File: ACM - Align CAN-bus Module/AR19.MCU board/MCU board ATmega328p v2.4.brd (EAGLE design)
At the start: 160 x 100 mm, 37 parts, among them IC1 ATMEGA328P-MMH, IC2 MIC5239-5.0YS_TR, IC3 MCP25625-E_ML, J1 AVR_SPI_PROG_3X2NS

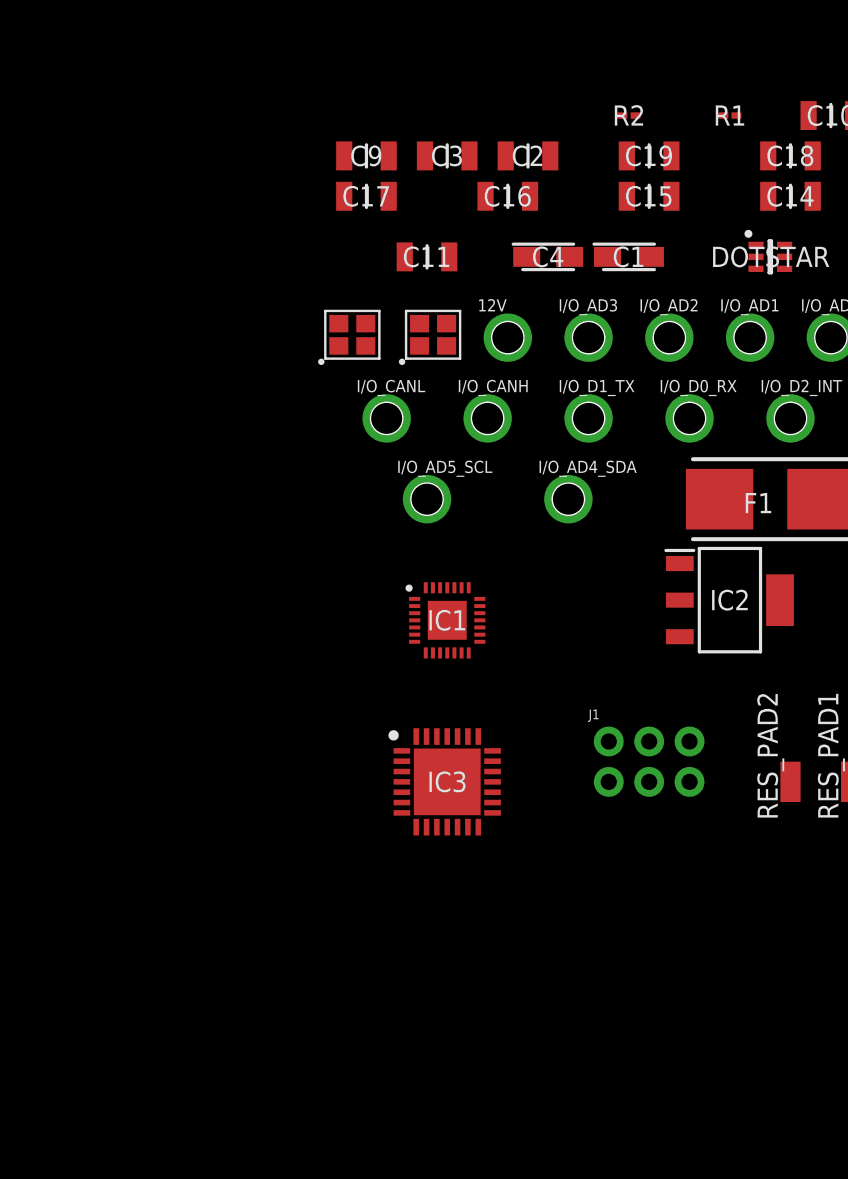
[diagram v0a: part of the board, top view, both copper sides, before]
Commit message: + SPI Priority | / 10K and 500Ohm to larger package | Smallest part 1206
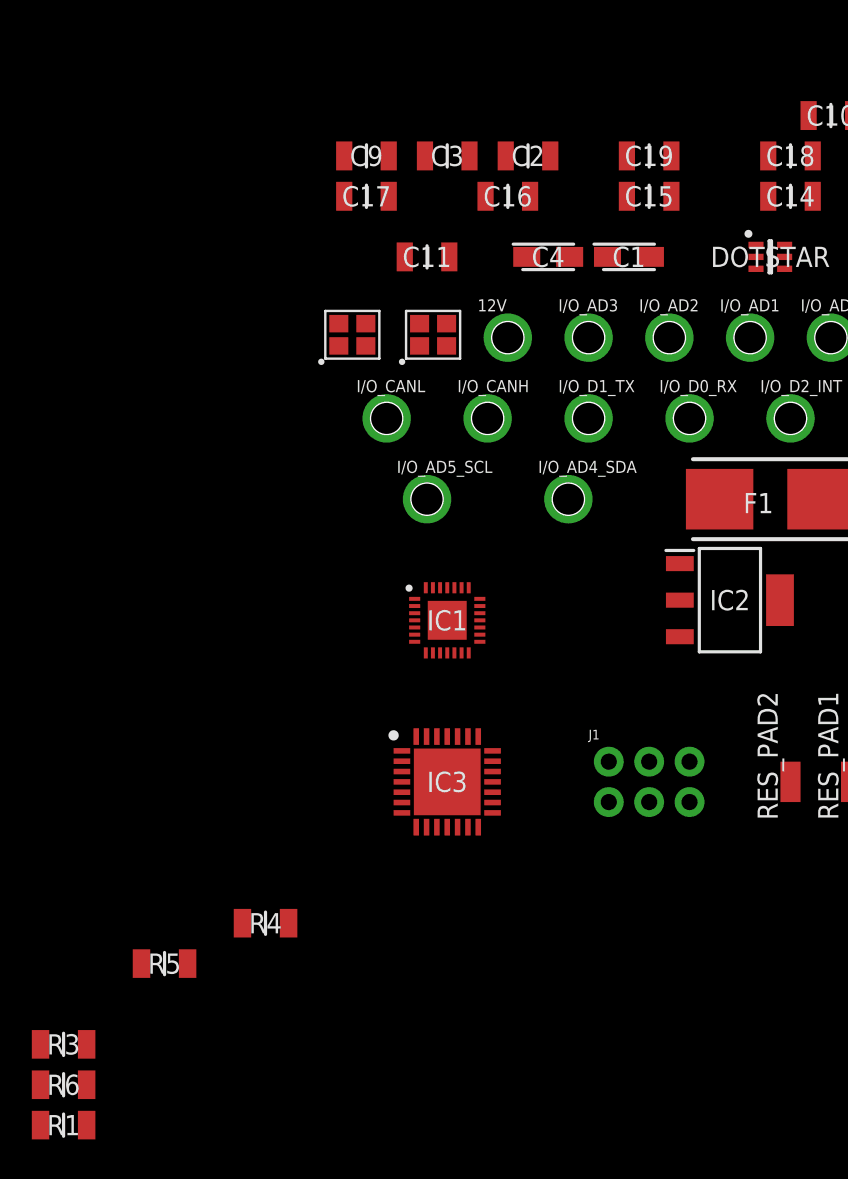
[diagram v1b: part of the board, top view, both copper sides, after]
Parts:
- removed R2: 10KΩ, CPF0201D10KC1:RESC0603X28N
- added R3, R4, R5: 500Ohm, CRCW1206499RFKEAHP(499ohm resistor):RESC3116X65N
- added R6: 10K Ohm, CRCW120610K0FKEAHP(10K Ohm):RESC3116X65N
- R1: value 10KΩ -> 10K Ohm; device CPF0201D10KC1:RESC0603X28N -> CRCW120610K0FKEAHP(10K Ohm):RESC3116X65N
- moved R1 76.1 mm to (-63.5, -17.8)
- moved J1 1.27 mm to (-26.7, 3.81)
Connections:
- removed net MISO: J1.1
- removed net MOSI: J1.4
- new net PROG_MISO: J1.1, R4.1
- new net PROG_MOSI: J1.4, R5.1
- new net PROG_SCK: J1.3, R3.1
- net 5V: now also R6.2; no longer R2.2
- net CAN_MISO: now also R4.2
- net CAN_MOSI: now also R5.2
- net MCP_RESET: now also R1.1; no longer R2.1
- net RESET_MCU: now also R6.1; no longer R1.1
- net SCK: now also R3.2; no longer J1.3

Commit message: Updated BOM and SPI Priority
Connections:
- net CAN_MISO: now also R4.1; no longer IC1.14, R4.2
- net CAN_MOSI: now also R5.1; no longer IC1.13, R5.2
- net PROG_MISO: now also IC1.14, R4.2; no longer R4.1
- net PROG_MOSI: now also IC1.13, R5.2; no longer R5.1
- net PROG_SCK: now also IC1.15, R3.2; no longer R3.1
- net SCK: now also R3.1; no longer IC1.15, R3.2
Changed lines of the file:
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@@
 </signal>
 <signal name="SCK">
-<contactref element="IC1" pad="15"/>
 <contactref element="DOTSTAR" pad="2"/>
 <contactref element="IC3" pad="26"/>
-<contactref element="R3" pad="2"/>
-<wire x1="-40.02" y1="6.66" x2="-62.05" y2="-12.7" width="0" layer="19" extent="1-1"/>
-<wire x1="-37.32" y1="12.62" x2="-40.02" y2="6.66" width="0" layer="19" extent="1-1"/>
-<wire x1="-19.95" y1="36.83" x2="-37.32" y2="12.62" width="0" layer="19" extent="1-1"/>
+<contactref element="R3" pad="1"/>
+<wire x1="-40.02" y1="6.66" x2="-64.95" y2="-12.7" width="0" layer="19" extent="1-1"/>
+<wire x1="-19.95" y1="36.83" x2="-40.02" y2="6.66" width="0" layer="19" extent="1-1"/>
 </signal>
 <signal name="CANL">
@@
 <signal name="CAN_MISO">
 <contactref element="IC3" pad="28"/>
-<contactref element="IC1" pad="14"/>
-<contactref element="R4" pad="2"/>
-<wire x1="-41.32" y1="6.66" x2="-49.35" y2="-5.08" width="0" layer="19" extent="1-1"/>
-<wire x1="-38.02" y1="11.92" x2="-41.32" y2="6.66" width="0" layer="19" extent="1-1"/>
+<contactref element="R4" pad="1"/>
+<wire x1="-41.32" y1="6.66" x2="-52.25" y2="-5.08" width="0" layer="19" extent="1-1"/>
 </signal>
 <signal name="CAN_MOSI">
 <contactref element="IC3" pad="27"/>
-<contactref element="IC1" pad="13"/>
-<contactref element="R5" pad="2"/>
-<wire x1="-40.67" y1="6.66" x2="-55.7" y2="-7.62" width="0" layer="19" extent="1-1"/>
-<wire x1="-38.47" y1="11.92" x2="-40.67" y2="6.66" width="0" layer="19" extent="1-1"/>
+<contactref element="R5" pad="1"/>
+<wire x1="-40.67" y1="6.66" x2="-58.6" y2="-7.62" width="0" layer="19" extent="1-1"/>
 </signal>
 <signal name="TXCAN">
@@
 </signal>
 <signal name="PROG_MISO">
-<contactref element="R4" pad="1"/>
 <contactref element="J1" pad="1"/>
-<wire x1="-29.21" y1="2.54" x2="-52.25" y2="-5.08" width="0" layer="19" extent="1-1"/>
+<contactref element="IC1" pad="14"/>
+<contactref element="R4" pad="2"/>
+<wire x1="-38.02" y1="11.92" x2="-49.35" y2="-5.08" width="0" layer="19" extent="1-1"/>
+<wire x1="-29.21" y1="2.54" x2="-38.02" y2="11.92" width="0" layer="19" extent="1-1"/>
 </signal>
 <signal name="PROG_MOSI">
-<contactref element="R5" pad="1"/>
 <contactref element="J1" pad="4"/>
-<wire x1="-26.67" y1="5.08" x2="-58.6" y2="-7.62" width="0" layer="19" extent="1-1"/>
+<contactref element="IC1" pad="13"/>
+<contactref element="R5" pad="2"/>
+<wire x1="-38.47" y1="11.92" x2="-55.7" y2="-7.62" width="0" layer="19" extent="1-1"/>
+<wire x1="-26.67" y1="5.08" x2="-38.47" y2="11.92" width="0" layer="19" extent="1-1"/>
 </signal>
 <signal name="PROG_SCK">
-<contactref element="R3" pad="1"/>
 <contactref element="J1" pad="3"/>
-<wire x1="-26.67" y1="2.54" x2="-64.95" y2="-12.7" width="0" layer="19" extent="1-1"/>
+<contactref element="IC1" pad="15"/>
+<contactref element="R3" pad="2"/>
+<wire x1="-37.32" y1="12.62" x2="-62.05" y2="-12.7" width="0" layer="19" extent="1-1"/>
+<wire x1="-26.67" y1="2.54" x2="-37.32" y2="12.62" width="0" layer="19" extent="1-1"/>
 </signal>
 </signals>

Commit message: New board
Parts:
- moved IC2 66.5 mm to (39.4, 41.9)
- moved C4 57.2 mm to (24.1, 39.4), turned to 90 degrees
- moved IC3 55.8 mm to (14.0, 20.3)
- moved IC1 54.6 mm to (12.7, 30.5)
- moved DOTSTAR 50.8 mm to (21.6, 6.35)
- moved F1 41.7 mm to (14.0, 47.0)
- moved J1 39.5 mm to (12.7, 6.35)
- moved 12V 31.9 mm to (-6.35, 44.5)
- moved R4 15.7 mm to (-35.6, -8.89)
- moved C1 9.67 mm to (-19.1, 33.0)
- moved C16 1.80 mm to (-34.3, 39.4)

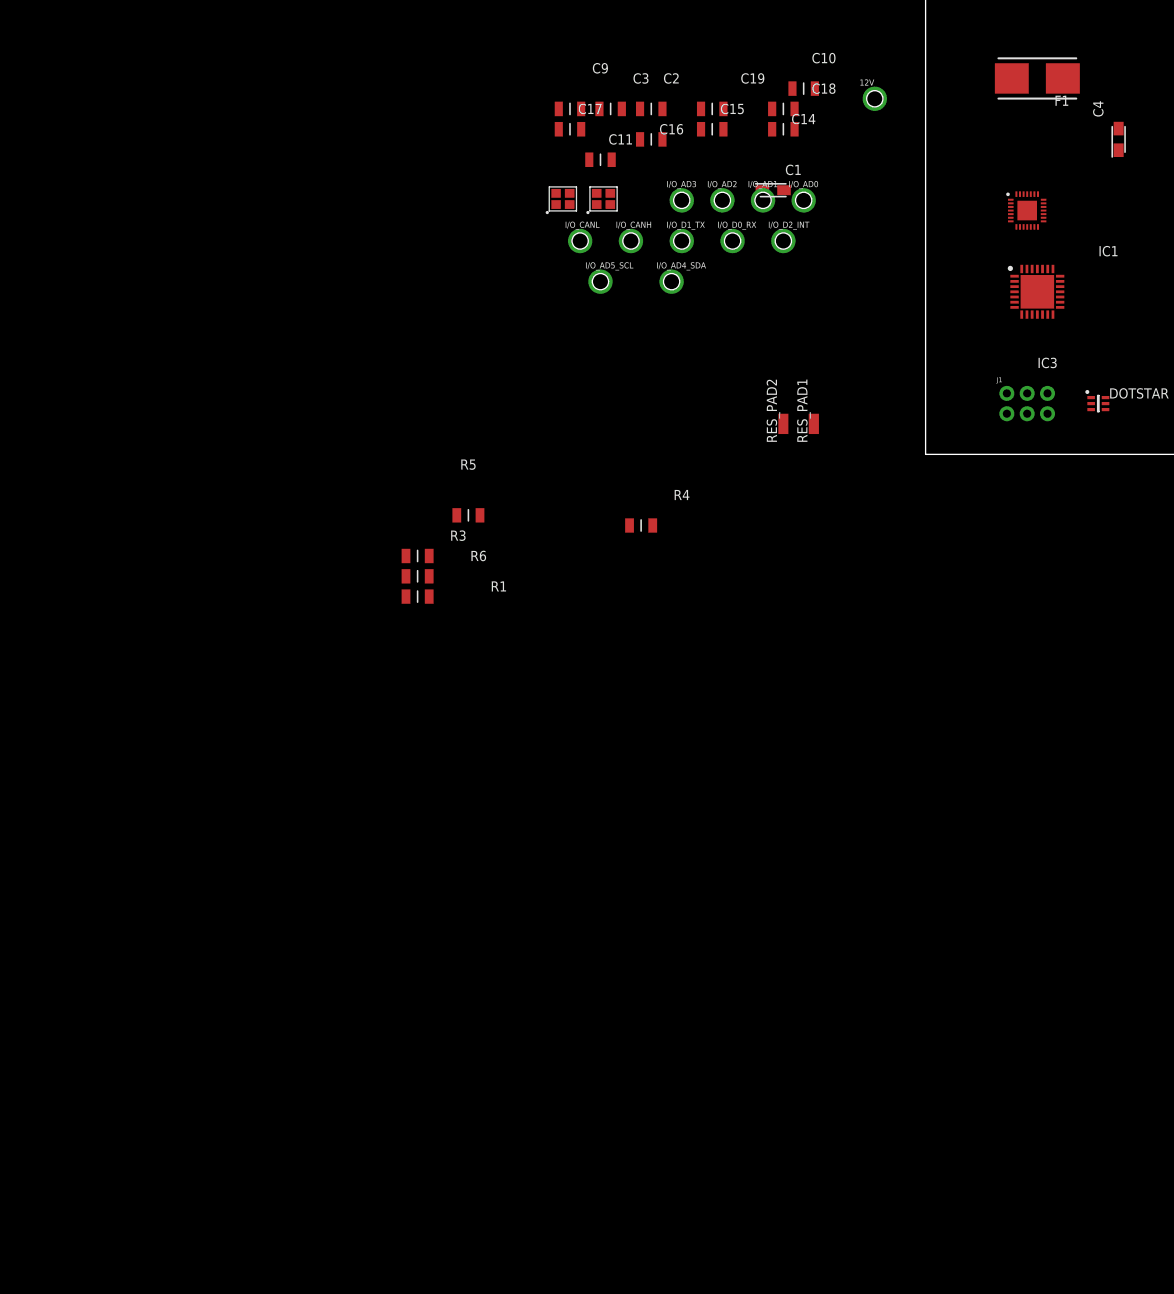
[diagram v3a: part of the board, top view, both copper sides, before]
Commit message: Byttet I/O pins, 0603 imp smd størrelse. Mangler dotstar support
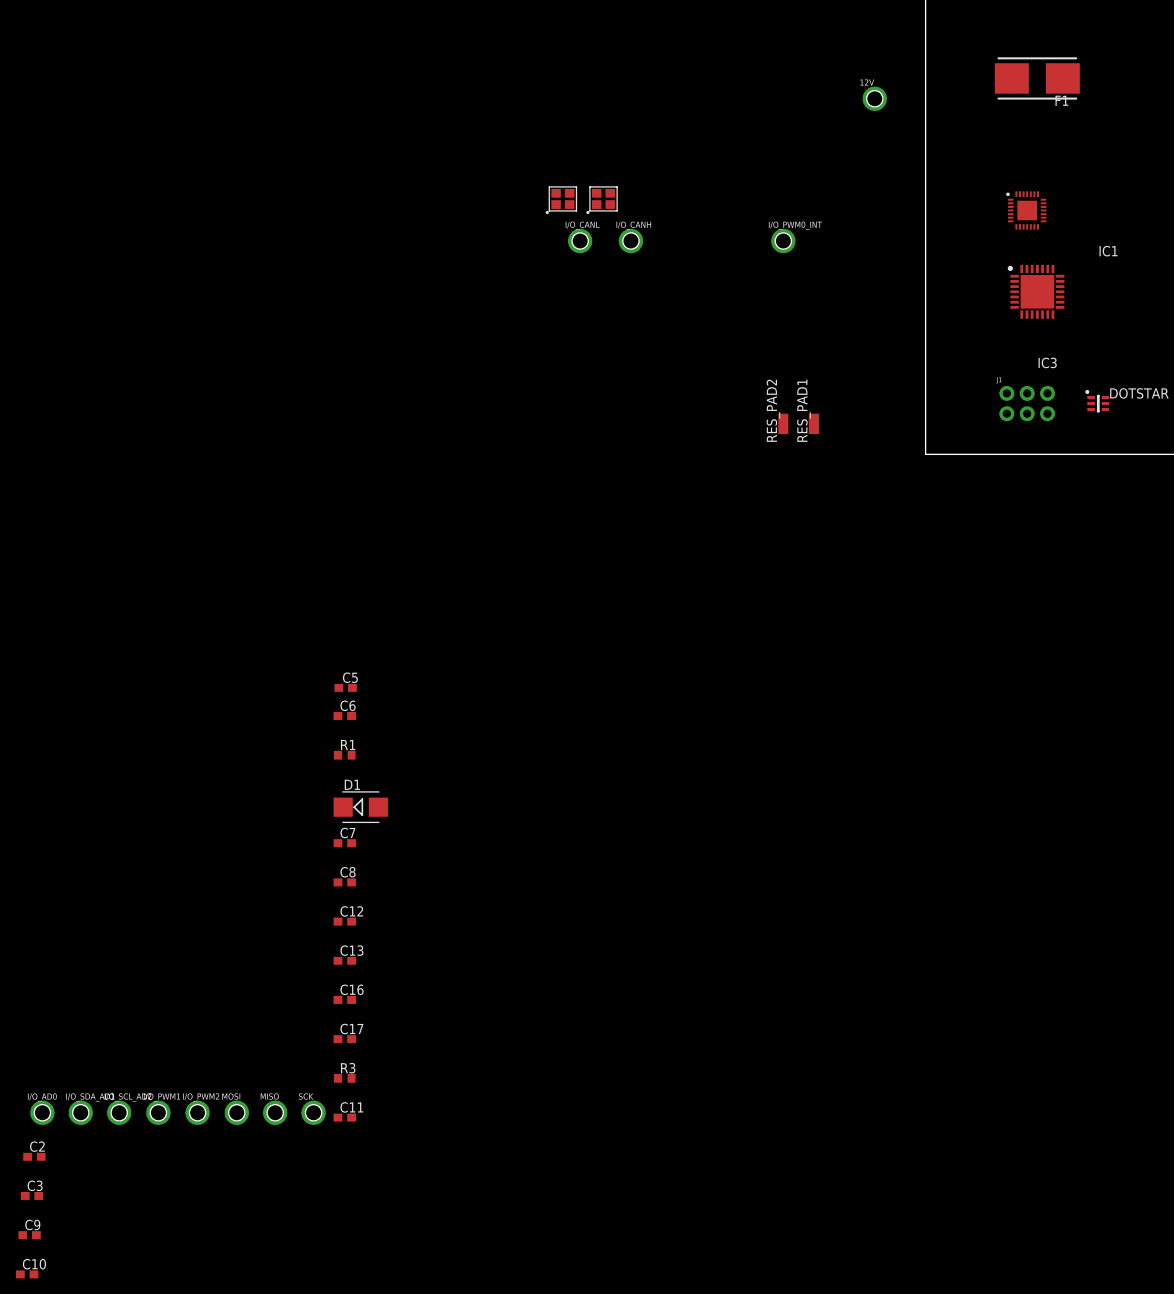
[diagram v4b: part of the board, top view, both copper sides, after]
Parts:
- removed C1, C4: 10uF, T491A106K016AT:CAPPM3216X180N
- removed C14, C15, C18, C19: 0.1uF_12, 12066D106KAT2A:CAPC3216X229N
- removed I/O_AD1, I/O_AD2, I/O_AD3, I/O_AD4_SDA, I/O_AD5_SCL, I/O_D0_RX, I/O_D1_TX: (no value), wirepad_edit:2,54/2,0(HALFHOLE)H+V
- removed R4, R5: 500Ohm, CRCW1206499RFKEAHP(499ohm resistor):RESC3116X65N
- removed R6: 10K Ohm, CRCW120610K0FKEAHP(10K Ohm):RESC3116X65N
- added C12, C13, C6, C7, C8: 0.1uF, eagle-ltspice:C0603
- added C5: 22pF, eagle-ltspice:C0603
- added D1: (no value), eagle-ltspice:DIODE_SMB
- added I/O_PWM1: I/O_PWM1, wirepad_edit:2,54/2,0(HALFHOLE)H+V
- added I/O_PWM2: I/O_PWM2, wirepad_edit:2,54/2,0(HALFHOLE)H+V
- added I/O_SCL_AD2: I/O_SCL_AD2, wirepad_edit:2,54/2,0(HALFHOLE)H+V
- added I/O_SDA_AD1: I/O_SDA_AD1, wirepad_edit:2,54/2,0(HALFHOLE)H+V
- added MISO: MISO, wirepad_edit:2,54/2,0(HALFHOLE)H+V
- added MOSI: MOSI, wirepad_edit:2,54/2,0(HALFHOLE)H+V
- added SCK: SCK, wirepad_edit:2,54/2,0(HALFHOLE)H+V
- 12V: value (none) -> 12V
- C10: value 22pF -> 10uF; device 12066D106KAT2A:CAPC3216X229N -> eagle-ltspice:C0603
- C11: value 0.1uF_12 -> 10uF; device 12066D106KAT2A:CAPC3216X229N -> eagle-ltspice:C0603
- C16, C17: value 0.1uF_12 -> 0.1uF; device 12066D106KAT2A:CAPC3216X229N -> eagle-ltspice:C0603
- C2, C3, C9: device 12066D106KAT2A:CAPC3216X229N -> eagle-ltspice:C0603
- I/O_AD0: value (none) -> I/O_AD0
- I/O_CANH, I/O_CANL: value (none) -> I/O_CANH
- I/O_PWM0_INT: value (none) -> I/O_PWM0_INT
- R1: value 10K Ohm -> 10kOhm; device CRCW120610K0FKEAHP(10K Ohm):RESC3116X65N -> eagle-ltspice:R0603
- R3: value 500Ohm -> 10kOhm; device CRCW1206499RFKEAHP(499ohm resistor):RESC3116X65N -> eagle-ltspice:R0603
- RES_PAD1: value (none) -> RES_PAD
- RES_PAD2: value (none) -> RES_PAD2
- moved C10 177.2 mm to (-112.3, -102.5)
- moved C9 156.1 mm to (-112.0, -97.6)
- moved C3 153.9 mm to (-111.7, -92.7)
- moved C2 152.0 mm to (-111.4, -87.8)
- moved I/O_AD0 148.5 mm to (-110.4, -82.3)
- moved C11 123.9 mm to (-72.6, -82.9)
- moved C17 117.2 mm to (-72.6, -73.1)
- moved C16 114.2 mm to (-72.6, -68.2)
- moved R3 65.9 mm to (-72.6, -78.0)
- moved R1 21.8 mm to (-72.6, -37.6)
- renumbered I/O_D2_INT to I/O_PWM0_INT
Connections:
- net CAN_INIT renamed CAN_INT
- removed net CAN_MISO: IC3.28, R4.1
- removed net CAN_MOSI: IC3.27, R5.1
- removed net I/O_AD0: I/O_AD0.P$1, IC1.19
- removed net I/O_AD1: I/O_AD1.P$1, IC1.20
- removed net I/O_AD2: I/O_AD2.P$1, IC1.21
- removed net I/O_AD3: I/O_AD3.P$1, IC1.22
- removed net I/O_AD4_SCL: I/O_AD4_SDA.P$1, IC1.23
- removed net I/O_AD5_SCL: I/O_AD5_SCL.P$1, IC1.24
- removed net I/O_D0_RX: I/O_D0_RX.P$1, IC1.26
- removed net I/O_D1_TX: I/O_D1_TX.P$1, IC1.27
- removed net MCP_RESET: C16.2, IC3.2, R1.1
- removed net PROG_MISO: IC1.14, J1.1, R4.2
- removed net PROG_MOSI: IC1.13, J1.4, R5.2
- removed net PROG_SCK: IC1.15, J1.3, R3.2
- new net MISO: IC1.14, IC3.27, J1.1, MISO.P$1
- new net MOSI: IC1.13, IC3.28, J1.4, MOSI.P$1
- new net N$1: IC3.2, R1.2
- new net N$2: I/O_PWM2.P$1, IC1.7
- new net N$3: I/O_PWM1.P$1, IC1.2
- new net N$5: I/O_AD0.P$1, IC1.22
- new net N$6: I/O_SDA_AD1.P$1, IC1.23
- new net N$7: I/O_SCL_AD2.P$1, IC1.24
- net 12V_FUSED: now also C10.1; no longer C4.2
- net 5V: now also C11.1, C12.1, C13.1, C16.1, C17.1, C6.1, C7.1, C8.1, D1.A, D1.C, R1.1, R3.2; no longer C1.1, C11.2, C14.2, C15.2, C17.2, C18.2, C19.2, R1.2, R6.2
- net CAN_CS: now also IC1.9; no longer IC1.11
- net CAN_OSC1: now also C5.1; no longer C9.2
- net CAN_OSC2: now also C2.1; no longer C10.2
- net DOTS_CS: no longer IC1.10
- net GND: now also C10.2, C11.2, C12.2, C13.2, C16.2, C17.2, C2.2, C3.2, C5.2, C6.2, C7.2, C8.2, C9.2; no longer C1.2, C10.1, C11.1, C14.1, C15.1, C16.1, C17.1, C18.1, C19.1, C2.1, C3.1, C4.1, C9.1
- net MCU_OSC1: now also C3.1; no longer C2.2
- net MCU_OSC2: now also C9.1; no longer C3.2
- net RESET_MCU: now also R3.1; no longer R6.1
- net SCK: now also IC1.15, J1.3, SCK.P$1; no longer R3.1

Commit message: Changes in schematic
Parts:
- removed D1: (no value), eagle-ltspice:DIODE_SMB
- removed DOTSTAR: COM-14608, APA102–2020:SON75P200X200X100-6N
- removed I/O_PWM1: I/O_PWM1, wirepad_edit:2,54/2,0(HALFHOLE)H+V
- removed I/O_PWM2: I/O_PWM2, wirepad_edit:2,54/2,0(HALFHOLE)H+V
- removed U$1, U$2: FA-20H, FA-20H 16.0000MF20X-B:FA-20H
- added C1: 0.1uF, eagle-ltspice:C0603
- added I/O_AD1: I/O_AD1, wirepad_edit:2,54/2,0(HALFHOLE)H+V
- added I/O_PWM0: I/O_PWM0, wirepad_edit:2,54/2,0(HALFHOLE)H+V
- added LED1: SMLP36RGB2W3R, SMLP36RGB2W3R:ROHM-1510-(0604)
- added R10, R2, R6, R7, R8, R9: 200Ohm, eagle-ltspice:R0603
- added R4: 290Ohm, eagle-ltspice:R0603
- added R5: 190Ohm, eagle-ltspice:R0603
- added U1, U2: CSTNE16M0V530000R0, CSTNE16M0V530000R0:CSTNE16M0V530000R0
- I/O_ADC2_SDA: value I/O_SDA_AD1 -> I/O_ADC2_SDA
- I/O_ADC3_SCL: value I/O_SCL_AD2 -> I/O_ADC3_SCL
- renumbered I/O_PWM0_INT to I/O_PWM1_INT1, I/O_SCL_AD2 to I/O_ADC3_SCL, I/O_SDA_AD1 to I/O_ADC2_SDA
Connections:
- removed net DOTS_CS: DOTSTAR.1
- new net BLUE_LED: IC1.11, R5.1
- new net GREEN_LED: IC1.8, R2.1
- new net N$10: R6.2, SCK.P$1
- new net N$11: MISO.P$1, R7.2
- new net N$12: MOSI.P$1, R8.2
- new net N$4: LED1.1, R2.2
- new net N$8: LED1.2, R4.2
- new net N$9: LED1.3, R5.2
- new net RED_LED: IC1.7, R4.1
- new net VOLTAGE_CHECK: C1.1, IC1.19, R10.2, R9.1
- net 12V_FUSED: now also R9.2
- net 5V: now also LED1.4, LED1.5, LED1.6; no longer D1.A, D1.C, DOTSTAR.4
- net CAN_OSC1: now also U1.1; no longer U$1.1
- net CAN_OSC2: now also U1.3; no longer U$1.3
- net GND: now also C1.2, R10.1, U1.2, U2.2; no longer DOTSTAR.3
- net MCU_OSC1: now also U2.1; no longer U$2.1
- net MCU_OSC2: now also U2.3; no longer U$2.3
- net MISO: now also R7.1; no longer MISO.P$1
- net MOSI: now also R8.1; no longer MOSI.P$1
- net N$2: now also I/O_PWM0.P$1, IC1.12; no longer I/O_PWM2.P$1, IC1.7
- net N$3: now also I/O_AD1.P$1, IC1.21; no longer I/O_PWM1.P$1, IC1.2
- net SCK: now also R6.1; no longer DOTSTAR.2, SCK.P$1
